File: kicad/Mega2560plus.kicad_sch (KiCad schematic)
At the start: 0 parts

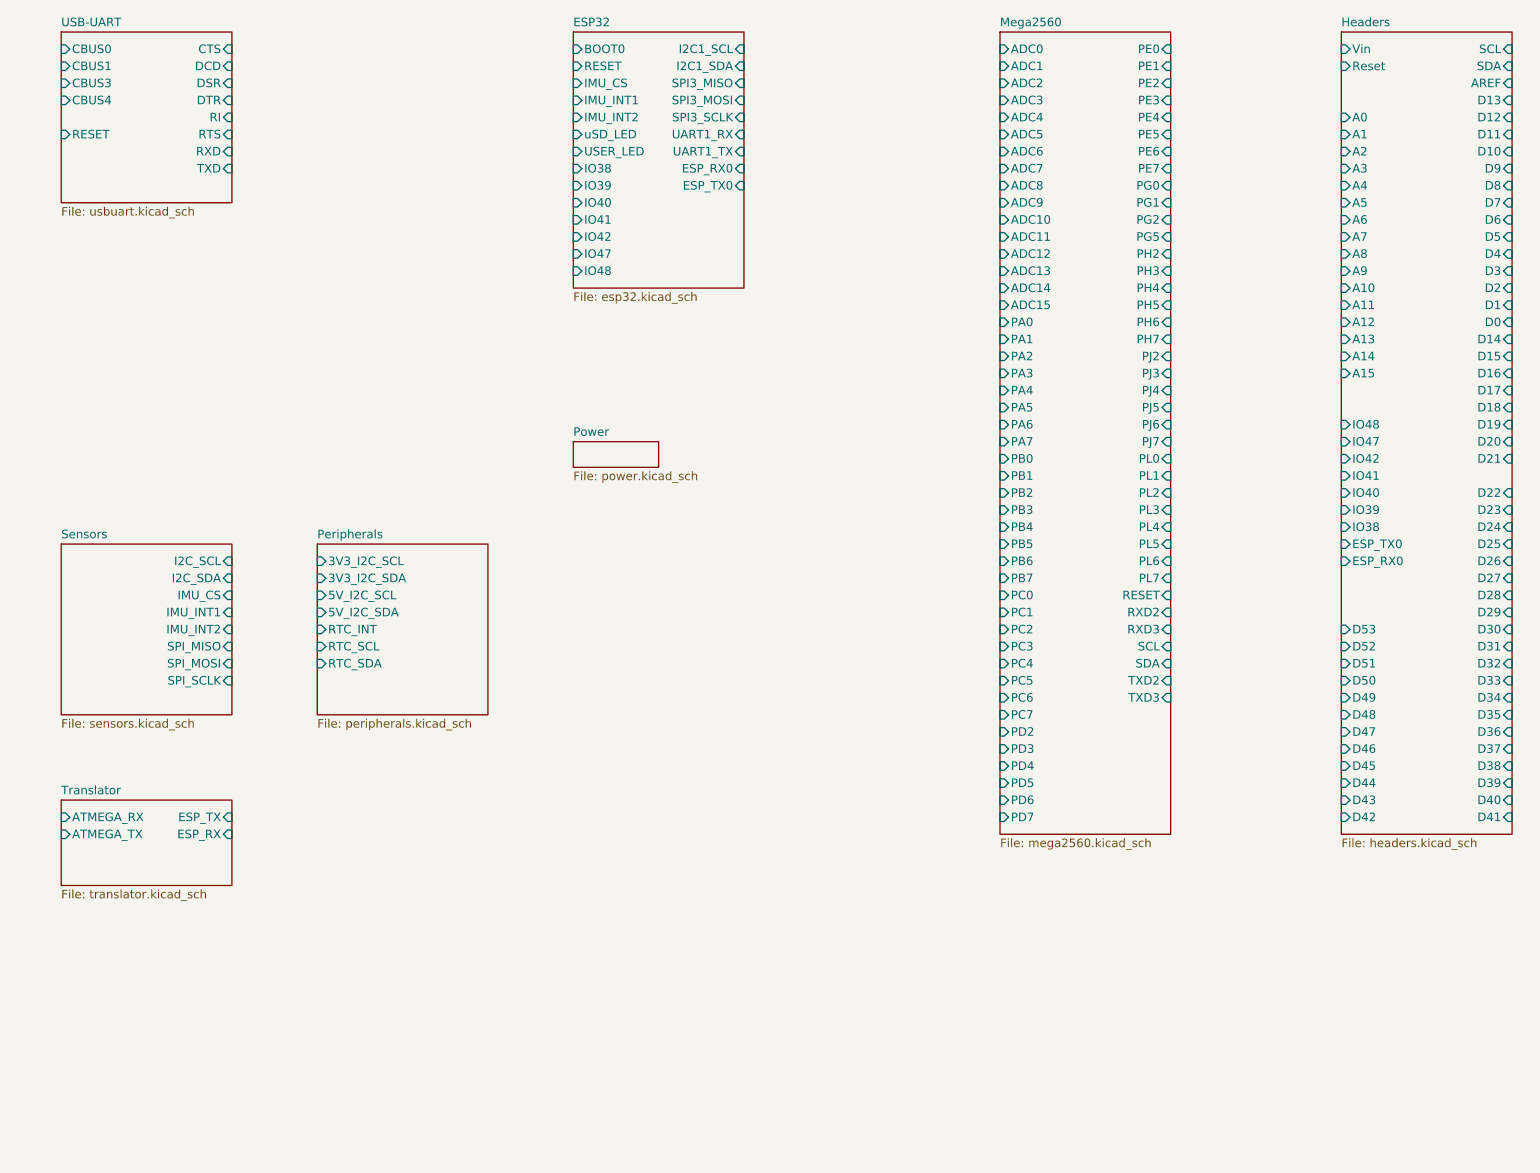
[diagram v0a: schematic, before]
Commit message: finished adding nets to mega2560 sheet
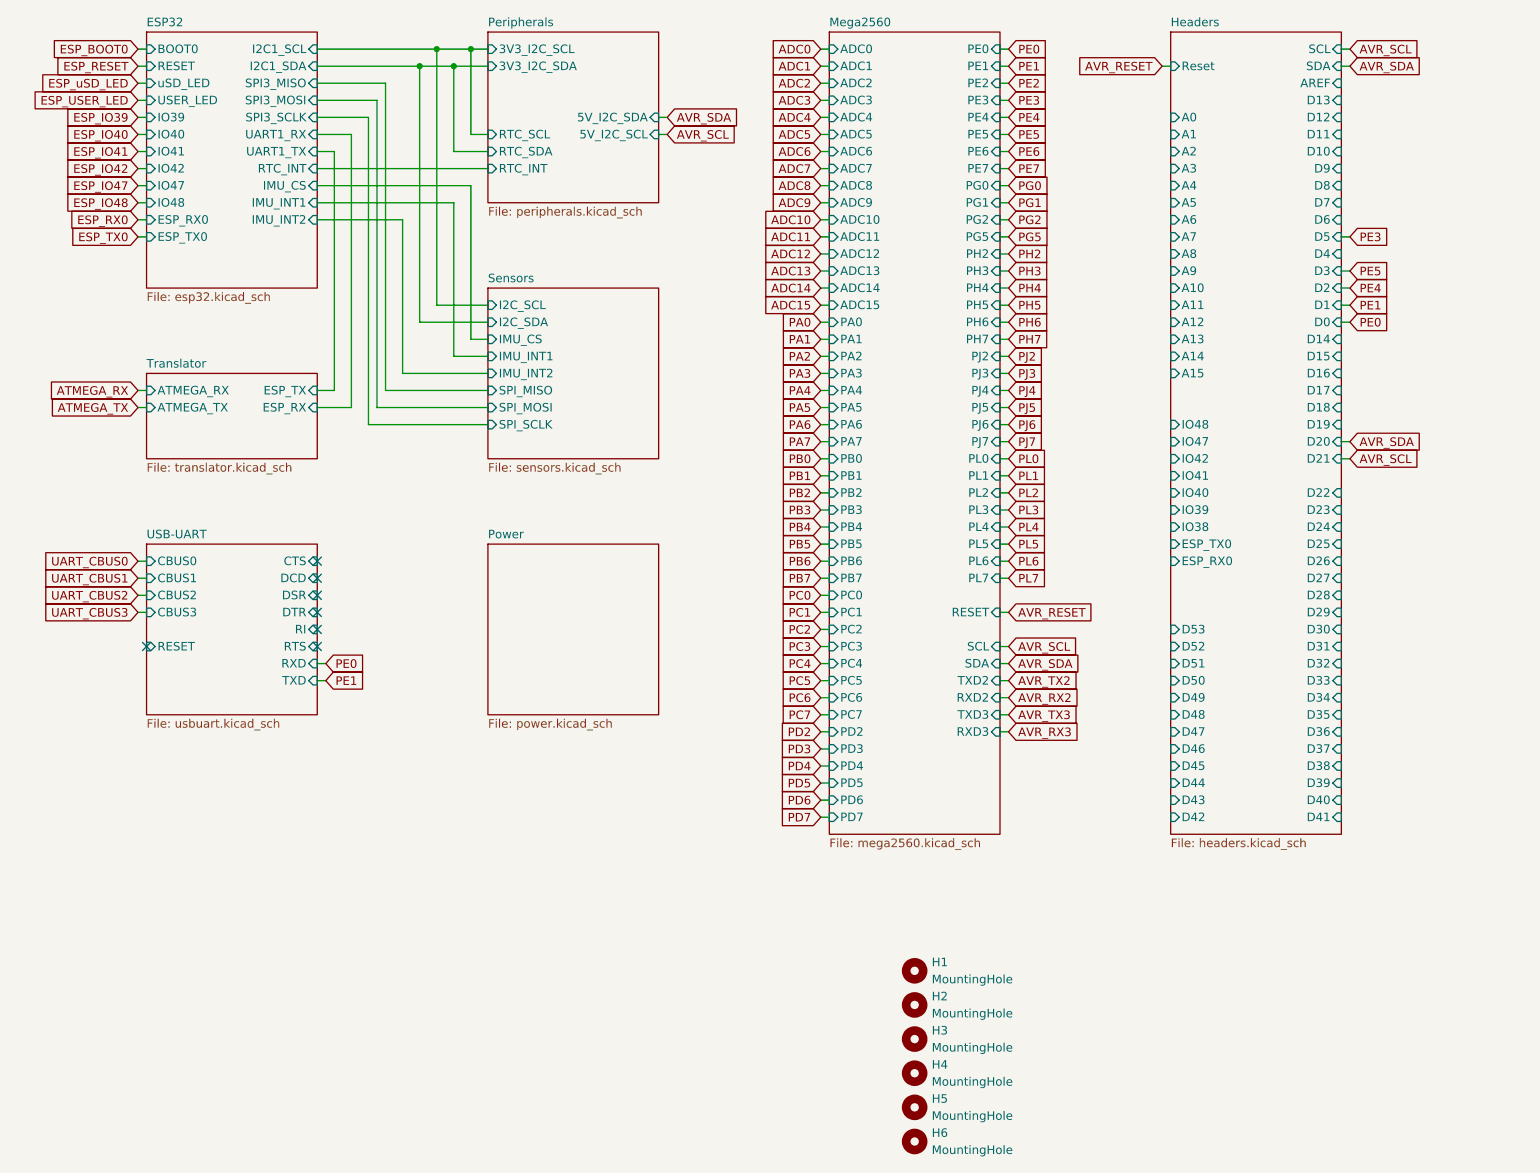
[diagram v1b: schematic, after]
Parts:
- added H1, H2, H3, H4, H5, H6: MountingHole, MountingHole:MountingHole_3.2mm_M3, symbol Mechanical:MountingHole
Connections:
- no-connect marks 0 -> 7
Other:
- sheet ESP32 ports: added RTC_INT; removed IO38
- sheet Headers ports: added none; removed Vin
- sheet USB-UART ports: added CBUS2; removed CBUS4
